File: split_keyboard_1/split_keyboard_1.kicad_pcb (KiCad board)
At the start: 2 copper layers, 111 x 89 mm, 64 parts, among them J1 B2B-PH-SM4-TB, SW1 SW_Push_45deg, SW10 SW_Push_45deg, SW11 SW_Push_45deg, SW12 SW_Push_45deg, SW13 SW_Push_45deg, SW14 SW_Push_45deg, SW15 SW_Push_45deg, SW16 SW_Push_45deg, SW17 SW_Push_45deg, SW18 SW_Push_45deg, SW19 SW_Push_45deg, SW2 SW_Push_45deg, SW20 SW_Push_45deg, SW21 SW_Push_45deg, SW22 SW_Push_45deg, SW23 SW_Push_45deg, SW24 SW_Push_45deg, SW25 SW_Push_45deg, SW26 SW_Push_45deg, SW27 SW_Push_45deg, SW28 SW_Push_45deg, SW29 SW_Push_45deg, SW3 SW_Push_45deg, SW30 SW_Push_45deg, SW32 SW_Push, SW4 SW_Push_45deg, SW5 SW_Push_45deg, SW6 SW_Push_45deg, SW7 SW_Push_45deg, SW8 SW_Push_45deg, SW9 SW_Push_45deg

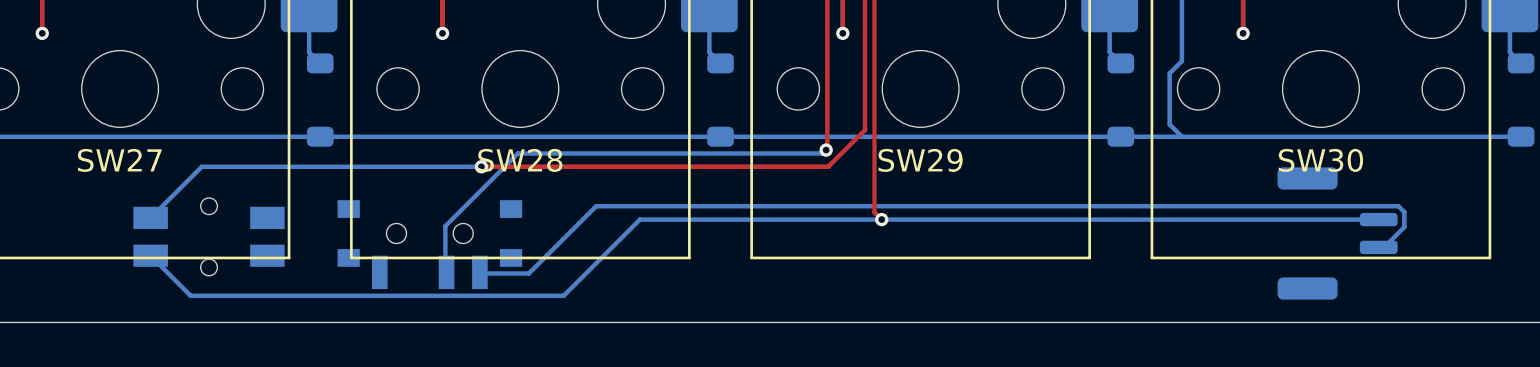
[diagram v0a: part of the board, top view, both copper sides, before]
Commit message: move switches to edge
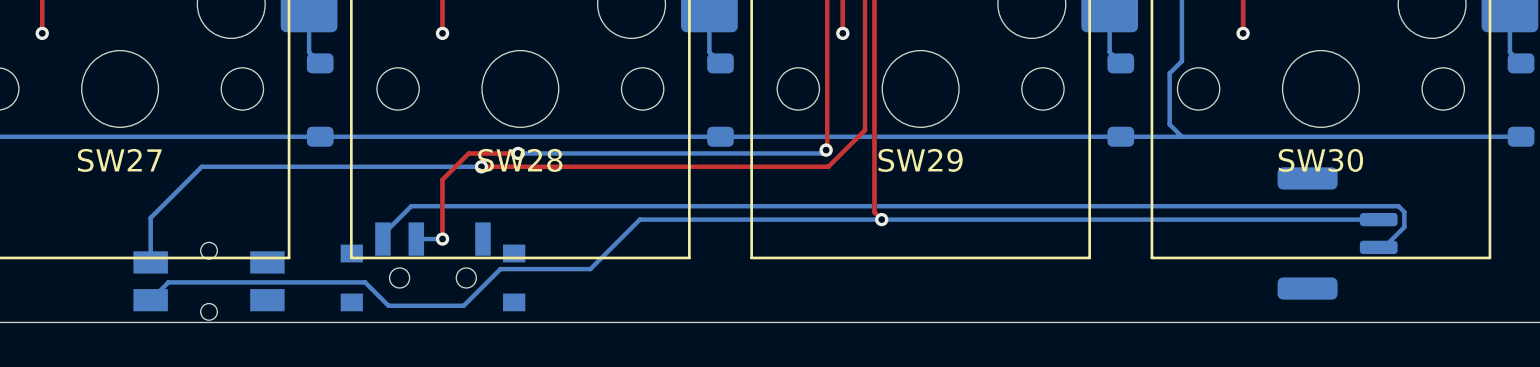
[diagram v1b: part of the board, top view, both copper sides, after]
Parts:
- moved SW31 2.19 mm to (149.8, 145.6), turned to 180 degrees
- moved SW32 2.00 mm to (139.8, 145.7)
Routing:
- net Net-(SW31-B): track 45.2 -> 49.0 mm
- net Net-(U1-RESET): track 82.8 -> 84.9 mm
- net Net-(SW31-C): track 71.9 -> 72.9 mm, vias 1 -> 3

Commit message: add ground plane
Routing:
- net GND: vias 4 -> 9
- added copper zone on B.Cu, net GND
- added copper zone on F.Cu, net GND
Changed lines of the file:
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@@
+	)
+	(segment
+		(start 183.75 73.449997)
+		(end 114.450003 73.449997)
+		(width 0.2)
+		(layer "F.Cu")
+		(net 45)
 	)
 	(segment
@@
 	(segment
 		(start 190.059997 73.449997)
-		(end 114.450003 73.449997)
+		(end 183.75 73.449997)
 		(width 0.2)
 		(layer "F.Cu")
@@
 	)
 	(via
+		(at 192 125.25)
+		(size 0.6)
+		(drill 0.3)
+		(layers "F.Cu" "B.Cu")
+		(free yes)
+		(net 50)
+	)
+	(via
+		(at 184 72)
+		(size 0.6)
+		(drill 0.3)
+		(layers "F.Cu" "B.Cu")
+		(free yes)
+		(net 50)
+	)
+	(via
 		(at 169.199 78.25)
 		(size 0.6)
@@
 	)
 	(via
+		(at 192.75 103.25)
+		(size 0.6)
+		(drill 0.3)
+		(layers "F.Cu" "B.Cu")
+		(free yes)
+		(net 50)
+	)
+	(via
+		(at 193.25 73.25)
+		(size 0.6)
+		(drill 0.3)
+		(layers "F.Cu" "B.Cu")
+		(net 50)
+	)
+	(via
 		(at 170.303265 94.075265)
 		(size 0.6)
 		(drill 0.3)
 		(layers "F.Cu" "B.Cu")
+		(net 50)
+	)
+	(via
+		(at 190.75 108.25)
+		(size 0.6)
+		(drill 0.3)
+		(layers "F.Cu" "B.Cu")
+		(free yes)
 		(net 50)
 	)
@@
 		(net 53)
 	)
+	(zone
+		(net 50)
+		(net_name "GND")
+		(layers "F.Cu" "B.Cu")
+		(hatch edge 0.5)
+		(connect_pads
+			(clearance 0.5)
+		)
+		(min_thickness 0.25)
+		(filled_areas_thickness no)
+		(fill yes
+			(thermal_gap 0.5)
+			(thermal_bridge_width 0.5)
+		)
+		(polygon
+			(pts
+				(xy 89.25 58.5) (xy 200.25 58.5) (xy 200.25 147.5) (xy 89.25 147.5)
+			)
+		)
+	)
 	(embedded_fonts no)
